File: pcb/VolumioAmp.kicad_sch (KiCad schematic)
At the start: 0 parts

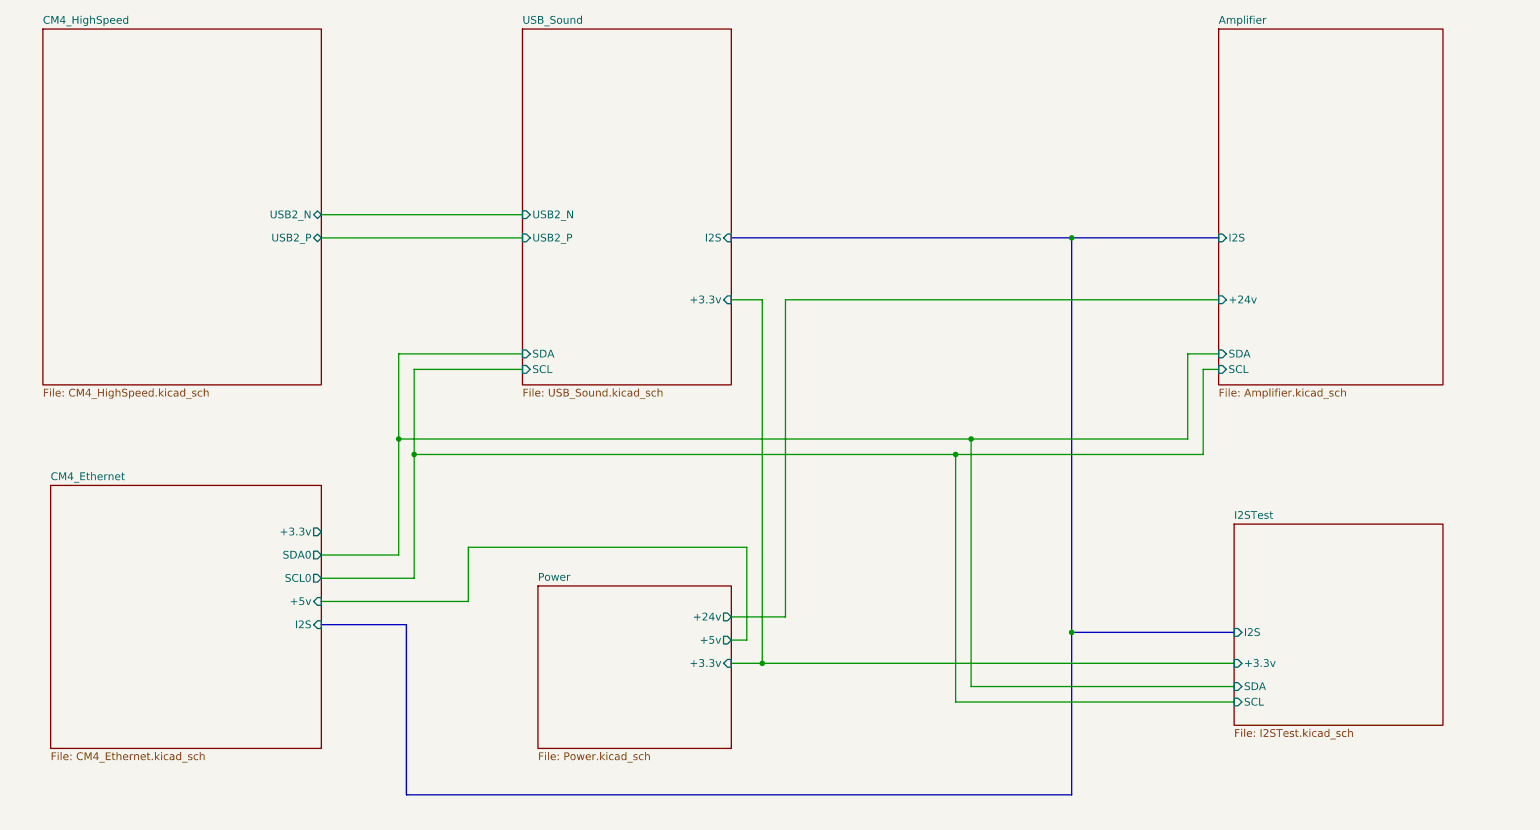
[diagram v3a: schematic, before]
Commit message: - amp connected
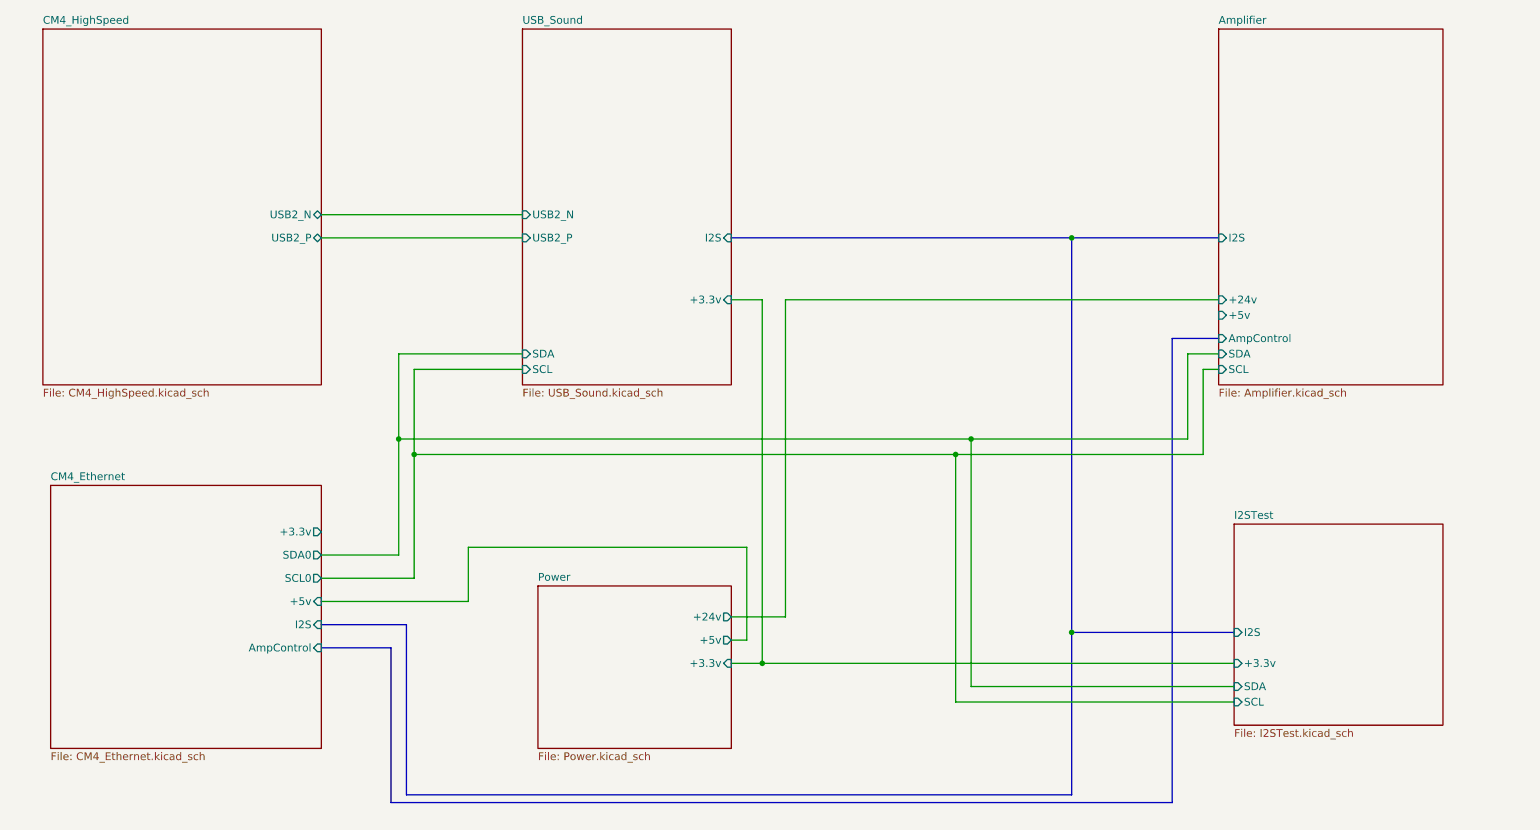
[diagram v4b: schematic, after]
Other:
- sheet Amplifier ports: added +5v, AmpControl; removed none
- sheet CM4_Ethernet ports: added AmpControl; removed none
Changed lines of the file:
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@@
+    (stroke (width 0) (type default))
+  )
+  (bus (pts (xy 82.55 133.35) (xy 93.98 133.35))
     (stroke (width 0) (type default))
   )
@@
     (stroke (width 0) (type default))
   )
+  (bus (pts (xy 222.25 82.55) (xy 229.87 82.55))
+    (stroke (width 0) (type default))
+  )
   (bus (pts (xy 205.74 130.81) (xy 205.74 157.48))
     (stroke (width 0) (type default))
   )
+  (bus (pts (xy 93.98 133.35) (xy 93.98 158.75))
+    (stroke (width 0) (type default))
+  )
   (wire (pts (xy 149.86 135.89) (xy 154.94 135.89))
     (stroke (width 0) (type default))
@@
     (stroke (width 0) (type default))
   )
+  (bus (pts (xy 222.25 158.75) (xy 222.25 82.55))
+    (stroke (width 0) (type default))
+  )
   (bus (pts (xy 205.74 66.04) (xy 205.74 130.81))
     (stroke (width 0) (type default))
@@
     (stroke (width 0) (type default))
   )
+  (bus (pts (xy 93.98 158.75) (xy 222.25 158.75))
+    (stroke (width 0) (type default))
+  )
   (wire (pts (xy 158.75 128.27) (xy 149.86 128.27))
     (stroke (width 0) (type default))
@@
       (effects (font (size 1.27 1.27)) (justify right))
     )
+    (pin "AmpControl" input (at 82.55 133.35 0)
+      (effects (font (size 1.27 1.27)) (justify right))
+    )
     (instances
       (project "VolumioAmp"
@@
       (effects (font (size 1.27 1.27)) (justify left))
     )
+    (pin "+5v" input (at 229.87 78.74 180)
+      (effects (font (size 1.27 1.27)) (justify left))
+    )
+    (pin "AmpControl" input (at 229.87 82.55 180)
+      (effects (font (size 1.27 1.27)) (justify left))
+    )

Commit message: - cleanup ERC errors
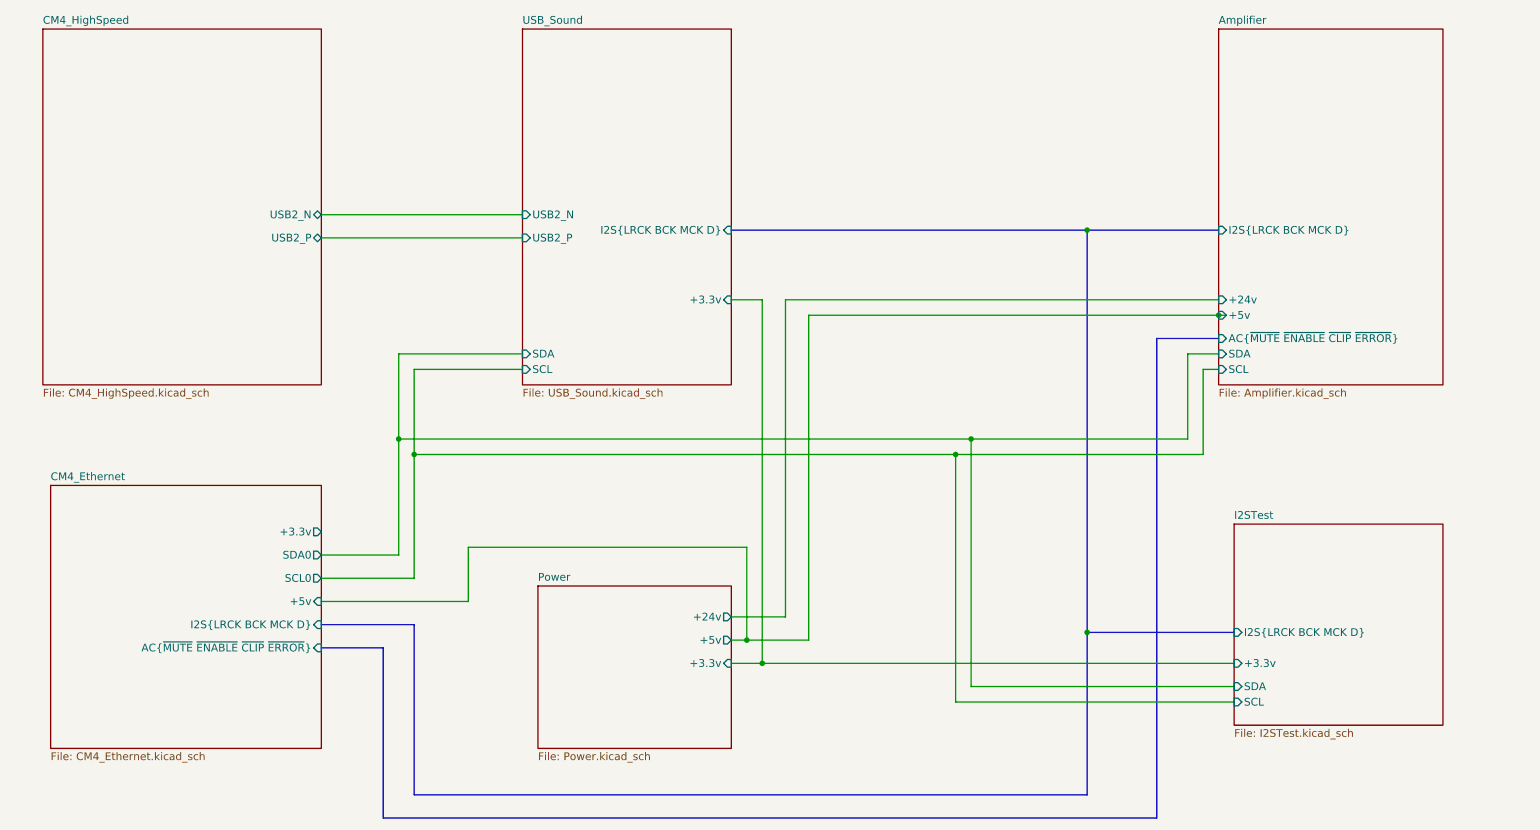
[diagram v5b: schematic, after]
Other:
- sheet Amplifier ports: added AC{~{MUTE} ~{ENABLE} ~{CLIP} ~{ERROR}}, I2S{LRCK BCK MCK D}; removed AmpControl, I2S
- sheet CM4_Ethernet ports: added AC{~{MUTE} ~{ENABLE} ~{CLIP} ~{ERROR}}, I2S{LRCK BCK MCK D}; removed AmpControl, I2S
- sheet I2STest ports: added I2S{LRCK BCK MCK D}; removed I2S
- sheet USB_Sound ports: added I2S{LRCK BCK MCK D}; removed I2S
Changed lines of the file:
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@@
 (kicad_sch (version 20230121) (generator eeschema)
   (paper "A4")
+  (junction (at 152.4 132.08) (diameter 0) (color 0 0 0 0)
+  )
   (junction (at 97.79 101.6) (diameter 0) (color 0 0 0 0)
   )
@@
   (junction (at 95.25 99.06) (diameter 0) (color 0 0 0 0)
   )
-  (junction (at 205.74 130.81) (diameter 0) (color 0 0 0 0)
+  (junction (at 229.87 78.74) (diameter 0) (color 0 0 0 0)
+  )
+  (junction (at 208.28 130.81) (diameter 0) (color 0 0 0 0)
   )
   (junction (at 186.69 101.6) (diameter 0) (color 0 0 0 0)
   )
-  (junction (at 205.74 66.04) (diameter 0) (color 0 0 0 0)
+  (junction (at 208.28 64.77) (diameter 0) (color 0 0 0 0)
+  )
+  (wire (pts (xy 231.14 78.74) (xy 229.87 78.74))
+    (stroke (width 0) (type default))
   )
   (wire (pts (xy 229.87 85.09) (xy 224.79 85.09))
@@
     (stroke (width 0) (type default))
   )
+  (bus (pts (xy 208.28 64.77) (xy 229.87 64.77))
+    (stroke (width 0) (type default))
+  )
+  (bus (pts (xy 208.28 157.48) (xy 97.79 157.48))
+    (stroke (width 0) (type default))
+  )
   (wire (pts (xy 154.94 76.2) (xy 154.94 135.89))
     (stroke (width 0) (type default))
   )
-  (bus (pts (xy 82.55 133.35) (xy 93.98 133.35))
-    (stroke (width 0) (type default))
-  )
   (wire (pts (xy 186.69 101.6) (xy 97.79 101.6))
     (stroke (width 0) (type default))
   )
+  (bus (pts (xy 208.28 64.77) (xy 208.28 130.81))
+    (stroke (width 0) (type default))
+  )
   (wire (pts (xy 82.55 66.04) (xy 115.57 66.04))
     (stroke (width 0) (type default))
   )
-  (bus (pts (xy 96.52 129.54) (xy 82.55 129.54))
+  (bus (pts (xy 149.86 64.77) (xy 208.28 64.77))
+    (stroke (width 0) (type default))
+  )
+  (wire (pts (xy 162.56 78.74) (xy 162.56 132.08))
     (stroke (width 0) (type default))
   )
@@
     (stroke (width 0) (type default))
   )
-  (bus (pts (xy 222.25 82.55) (xy 229.87 82.55))
-    (stroke (width 0) (type default))
-  )
-  (bus (pts (xy 205.74 130.81) (xy 205.74 157.48))
-    (stroke (width 0) (type default))
-  )
-  (bus (pts (xy 93.98 133.35) (xy 93.98 158.75))
+  (bus (pts (xy 208.28 130.81) (xy 208.28 157.48))
     (stroke (width 0) (type default))
   )
@@
     (stroke (width 0) (type default))
   )
-  (bus (pts (xy 96.52 157.48) (xy 96.52 129.54))
-    (stroke (width 0) (type default))
-  )
   (wire (pts (xy 95.25 99.06) (xy 95.25 85.09))
     (stroke (width 0) (type default))
@@
     (stroke (width 0) (type default))
   )
+  (bus (pts (xy 92.71 161.29) (xy 219.71 161.29))
+    (stroke (width 0) (type default))
+  )
+  (bus (pts (xy 208.28 130.81) (xy 232.41 130.81))
+    (stroke (width 0) (type default))
+  )
   (wire (pts (xy 82.55 125.73) (xy 106.68 125.73))
     (stroke (width 0) (type default))
@@
     (stroke (width 0) (type default))
   )
-  (bus (pts (xy 222.25 158.75) (xy 222.25 82.55))
-    (stroke (width 0) (type default))
-  )
-  (bus (pts (xy 205.74 66.04) (xy 205.74 130.81))
+  (bus (pts (xy 82.55 129.54) (xy 97.79 129.54))
+    (stroke (width 0) (type default))
+  )
+  (bus (pts (xy 219.71 82.55) (xy 229.87 82.55))
+    (stroke (width 0) (type default))
+  )
+  (bus (pts (xy 82.55 133.35) (xy 92.71 133.35))
+    (stroke (width 0) (type default))
+  )
+  (wire (pts (xy 229.87 78.74) (xy 162.56 78.74))
     (stroke (width 0) (type default))
   )
@@
     (stroke (width 0) (type default))
   )
-  (bus (pts (xy 149.86 66.04) (xy 205.74 66.04))
-    (stroke (width 0) (type default))
-  )
-  (bus (pts (xy 205.74 157.48) (xy 96.52 157.48))
-    (stroke (width 0) (type default))
-  )
   (wire (pts (xy 149.86 132.08) (xy 152.4 132.08))
     (stroke (width 0) (type default))
@@
     (stroke (width 0) (type default))
   )
-  (bus (pts (xy 93.98 158.75) (xy 222.25 158.75))
+  (bus (pts (xy 92.71 133.35) (xy 92.71 161.29))
     (stroke (width 0) (type default))
   )
@@
     (stroke (width 0) (type default))
   )
-  (bus (pts (xy 205.74 66.04) (xy 229.87 66.04))
-    (stroke (width 0) (type default))
-  )
   (wire (pts (xy 229.87 87.63) (xy 227.33 87.63))
     (stroke (width 0) (type default))
   )
+  (wire (pts (xy 162.56 132.08) (xy 152.4 132.08))
+    (stroke (width 0) (type default))
+  )
+  (bus (pts (xy 97.79 157.48) (xy 97.79 129.54))
+    (stroke (width 0) (type default))
+  )
   (wire (pts (xy 95.25 118.11) (xy 95.25 99.06))
     (stroke (width 0) (type default))
@@
     (stroke (width 0) (type default))
   )
-  (bus (pts (xy 205.74 130.81) (xy 232.41 130.81))
+  (bus (pts (xy 219.71 161.29) (xy 219.71 82.55))
     (stroke (width 0) (type default))
   )
@@
       (effects (font (size 1.27 1.27)) (justify right))
     )
-    (pin "I2S" input (at 82.55 129.54 0)
-      (effects (font (size 1.27 1.27)) (justify right))
-    )
-    (pin "AmpControl" input (at 82.55 133.35 0)
+    (pin "AC{~{MUTE} ~{ENABLE} ~{CLIP} ~{ERROR}}" input (at 82.55 133.35 0)
+      (effects (font (size 1.27 1.27)) (justify right))
+    )
+    (pin "I2S{LRCK BCK MCK D}" input (at 82.55 129.54 0)
       (effects (font (size 1.27 1.27)) (justify right))
     )
@@
       (effects (font (size 1.27 1.27)) (justify left))
     )
-    (pin "I2S" input (at 232.41 130.81 180)
+    (pin "I2S{LRCK BCK MCK D}" input (at 232.41 130.81 180)
       (effects (font (size 1.27 1.27)) (justify left))
     )
@@
       (effects (font (size 1.27 1.27)) (justify left))
     )
-    (pin "I2S" input (at 149.86 66.04 0)
+    (pin "I2S{LRCK BCK MCK D}" input (at 149.86 64.77 0)
       (effects (font (size 1.27 1.27)) (justify right))
     )
@@
       (effects (font (size 1.27 1.27)) (justify left))
     )
-    (pin "I2S" input (at 229.87 66.04 180)
-      (effects (font (size 1.27 1.27)) (justify left))
-    )
     (pin "+5v" input (at 229.87 78.74 180)
       (effects (font (size 1.27 1.27)) (justify left))
     )
-    (pin "AmpControl" input (at 229.87 82.55 180)
-      (effects (font (size 1.27 1.27)) (justify left))
-    )
+    (pin "AC{~{MUTE} ~{ENABLE} ~{CLIP} ~{ERROR}}" input (at 229.87 82.55 180)
+      (effects (font (size 1.27 1.27)) (justify left))
+    )
+    (pin "I2S{LRCK BCK MCK D}" input (at 229.87 64.77 180)
+      (effects (font (size 1.27 1.27)) (justify left))
+    )

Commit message: - ERC checks
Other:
- sheet CM4_Ethernet ports: added none; removed +3.3v
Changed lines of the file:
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@@
       (effects (font (size 1.27 1.27)) (justify left top))
-    )
-    (pin "+3.3v" output (at 82.55 114.3 0)
-      (effects (font (size 1.27 1.27)) (justify right))
     )
     (pin "SDA0" output (at 82.55 118.11 0)
